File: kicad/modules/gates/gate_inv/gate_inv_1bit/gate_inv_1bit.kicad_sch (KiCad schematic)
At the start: 2 parts, among them Q101 PMOS, Q102 NMOS

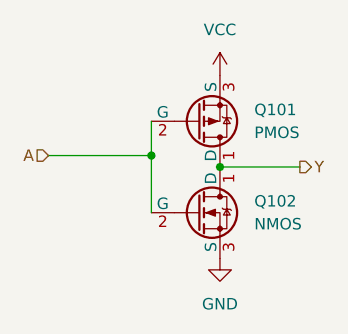
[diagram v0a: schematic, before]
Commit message: feat: complete circuit designs for all ALU components
* Designed all gate modules: AND, OR, NOT, NAND, NOR, XOR (1-bit and 8-bit variants)

* Completed multiplexer hierarchy: 2:1, 4:1, and 8:1 8-bit muxes

* Finalized add_sub board schematic and LED panel designs

* Added new board modules: flags, main_control, main_logic

* Updated Logisim top-level ALU circuit

* Note: KiCad directory path errors to be resolved next (iCloud sync issue), then begin PCB routing
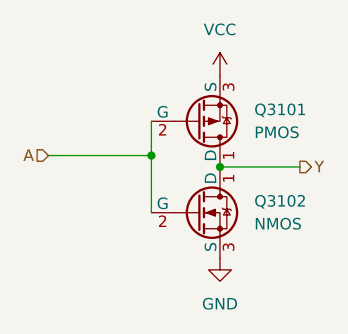
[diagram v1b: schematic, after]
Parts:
- renumbered Q101 to Q3101, Q102 to Q3102
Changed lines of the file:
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@@
 		(dnp no)
 		(fields_autoplaced yes)
-		(property "Reference" "Q102"
+		(property "Reference" "Q3102"
 			(at 102.87 63.4999 0)
 			(effects
@@
 		)
 		(instances
-			(project ""
-				(path "/91c6beb6-7f64-405a-ad9b-2f4d375cbae0"
-					(reference "Q102")
+			(project "main_logic"
+				(path "/9c59990f-2fe5-4da7-bc07-d03b445b1465/99dbd45c-8760-4ff5-9139-add98e67407e"
+					(reference "Q3102")
+					(unit 1)
+				)
+			)
+			(project "main_logic"
+				(path "/e2bb65ff-e340-4712-a878-121a5433abf0/c953f248-6ec6-4063-88a9-6cf78c9a3ffe"
+					(reference "Q3102")
 					(unit 1)
 				)
@@
 		(dnp no)
 		(fields_autoplaced yes)
-		(property "Reference" "#PWR0101"
+		(property "Reference" "#PWR03102"
 			(at 99.06 76.2 0)
 			(effects
@@
 		)
 		(instances
-			(project ""
-				(path "/91c6beb6-7f64-405a-ad9b-2f4d375cbae0"
-					(reference "#PWR0101")
+			(project "main_logic"
+				(path "/9c59990f-2fe5-4da7-bc07-d03b445b1465/99dbd45c-8760-4ff5-9139-add98e67407e"
+					(reference "#PWR03102")
+					(unit 1)
+				)
+			)
+			(project "main_logic"
+				(path "/e2bb65ff-e340-4712-a878-121a5433abf0/c953f248-6ec6-4063-88a9-6cf78c9a3ffe"
+					(reference "#PWR03102")
 					(unit 1)
 				)
@@
 		(dnp no)
 		(fields_autoplaced yes)
-		(property "Reference" "Q101"
+		(property "Reference" "Q3101"
 			(at 102.87 53.3399 0)
 			(effects
@@
 		)
 		(instances
-			(project ""
-				(path "/91c6beb6-7f64-405a-ad9b-2f4d375cbae0"
-					(reference "Q101")
+			(project "main_logic"
+				(path "/9c59990f-2fe5-4da7-bc07-d03b445b1465/99dbd45c-8760-4ff5-9139-add98e67407e"
+					(reference "Q3101")
+					(unit 1)
+				)
+			)
+			(project "main_logic"
+				(path "/e2bb65ff-e340-4712-a878-121a5433abf0/c953f248-6ec6-4063-88a9-6cf78c9a3ffe"
+					(reference "Q3101")
 					(unit 1)
 				)
@@
 		(dnp no)
 		(fields_autoplaced yes)
-		(property "Reference" "#PWR0102"
+		(property "Reference" "#PWR03101"
 			(at 99.06 53.34 0)
 			(effects
@@
 		)
 		(instances
-			(project ""
-				(path "/91c6beb6-7f64-405a-ad9b-2f4d375cbae0"
-					(reference "#PWR0102")
+			(project "main_logic"
+				(path "/9c59990f-2fe5-4da7-bc07-d03b445b1465/99dbd45c-8760-4ff5-9139-add98e67407e"
+					(reference "#PWR03101")
+					(unit 1)
+				)
+			)
+			(project "main_logic"
+				(path "/e2bb65ff-e340-4712-a878-121a5433abf0/c953f248-6ec6-4063-88a9-6cf78c9a3ffe"
+					(reference "#PWR03101")
 					(unit 1)
 				)
@@
 		)
 	)
-	(sheet_instances
-		(path "/"
-			(page "1")
-		)
-	)
-	(embedded_fonts no)
 )

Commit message: Fix KiCad file paths and complete core circuit design
- Fixed file path errors across all KiCad schematics and projects
- Completed core circuit designs:
  * Adder and subtractor modules (adder2, adder8)
  * LED panels (led_panel_1) with display circuits
  * Flag LED circuits for status indicators
  * All dependent logic gate modules (AND, OR, NOT, NAND, NOR, XOR)
  * All multiplexer modules (2:1, 4:1, 8:1, 8-bit)
  * Main control board schematics
  * Flags board schematics
- Updated .gitignore to exclude KiCad backups, cache files, and lock files
- Ready for pin placement and routing of control buses, power rails, and inter-board signals
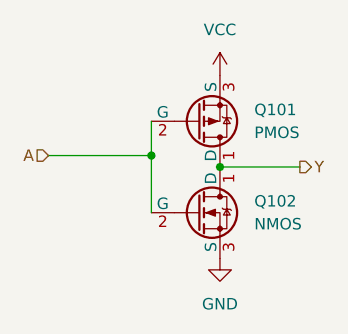
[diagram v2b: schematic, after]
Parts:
- renumbered Q3101 to Q101, Q3102 to Q102
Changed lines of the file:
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@@
 		(dnp no)
 		(fields_autoplaced yes)
-		(property "Reference" "Q3102"
+		(property "Reference" "Q102"
 			(at 102.87 63.4999 0)
 			(effects
@@
 		)
 		(instances
-			(project "main_logic"
-				(path "/9c59990f-2fe5-4da7-bc07-d03b445b1465/99dbd45c-8760-4ff5-9139-add98e67407e"
-					(reference "Q3102")
-					(unit 1)
-				)
-			)
-			(project "main_logic"
-				(path "/e2bb65ff-e340-4712-a878-121a5433abf0/c953f248-6ec6-4063-88a9-6cf78c9a3ffe"
-					(reference "Q3102")
+			(project "gate_inv_8bit"
+				(path "/d141fce1-7092-474f-ac13-21228438d92c/12baccda-de61-4ff2-89c1-cc980ff8bc59"
+					(reference "Q402")
+					(unit 1)
+				)
+				(path "/d141fce1-7092-474f-ac13-21228438d92c/3a2fa2a6-4027-46c4-90cc-58cbe339a8cc"
+					(reference "Q302")
+					(unit 1)
+				)
+				(path "/d141fce1-7092-474f-ac13-21228438d92c/60421d18-f918-422e-9acf-6291f4552ab2"
+					(reference "Q102")
+					(unit 1)
+				)
+				(path "/d141fce1-7092-474f-ac13-21228438d92c/7ca7b9d9-dd96-40f5-80e5-151f81d53068"
+					(reference "Q502")
+					(unit 1)
+				)
+				(path "/d141fce1-7092-474f-ac13-21228438d92c/cbe845e2-fbfa-4e99-b5aa-42ea773ed407"
+					(reference "Q802")
+					(unit 1)
+				)
+				(path "/d141fce1-7092-474f-ac13-21228438d92c/cfb92fbf-905c-43ce-8707-6acd4a04428b"
+					(reference "Q602")
+					(unit 1)
+				)
+				(path "/d141fce1-7092-474f-ac13-21228438d92c/e8076ae0-d234-4675-a580-3fff14bf2f4c"
+					(reference "Q702")
 					(unit 1)
 				)
@@
 		(dnp no)
 		(fields_autoplaced yes)
-		(property "Reference" "#PWR03102"
+		(property "Reference" "#PWR0102"
 			(at 99.06 76.2 0)
 			(effects
@@
 		)
 		(instances
-			(project "main_logic"
-				(path "/9c59990f-2fe5-4da7-bc07-d03b445b1465/99dbd45c-8760-4ff5-9139-add98e67407e"
-					(reference "#PWR03102")
-					(unit 1)
-				)
-			)
-			(project "main_logic"
-				(path "/e2bb65ff-e340-4712-a878-121a5433abf0/c953f248-6ec6-4063-88a9-6cf78c9a3ffe"
-					(reference "#PWR03102")
+			(project "gate_inv_8bit"
+				(path "/d141fce1-7092-474f-ac13-21228438d92c/12baccda-de61-4ff2-89c1-cc980ff8bc59"
+					(reference "#PWR0402")
+					(unit 1)
+				)
+				(path "/d141fce1-7092-474f-ac13-21228438d92c/3a2fa2a6-4027-46c4-90cc-58cbe339a8cc"
+					(reference "#PWR0302")
+					(unit 1)
+				)
+				(path "/d141fce1-7092-474f-ac13-21228438d92c/60421d18-f918-422e-9acf-6291f4552ab2"
+					(reference "#PWR0102")
+					(unit 1)
+				)
+				(path "/d141fce1-7092-474f-ac13-21228438d92c/7ca7b9d9-dd96-40f5-80e5-151f81d53068"
+					(reference "#PWR0502")
+					(unit 1)
+				)
+				(path "/d141fce1-7092-474f-ac13-21228438d92c/cbe845e2-fbfa-4e99-b5aa-42ea773ed407"
+					(reference "#PWR0802")
+					(unit 1)
+				)
+				(path "/d141fce1-7092-474f-ac13-21228438d92c/cfb92fbf-905c-43ce-8707-6acd4a04428b"
+					(reference "#PWR0602")
+					(unit 1)
+				)
+				(path "/d141fce1-7092-474f-ac13-21228438d92c/e8076ae0-d234-4675-a580-3fff14bf2f4c"
+					(reference "#PWR0702")
 					(unit 1)
 				)
@@
 		(dnp no)
 		(fields_autoplaced yes)
-		(property "Reference" "Q3101"
+		(property "Reference" "Q101"
 			(at 102.87 53.3399 0)
 			(effects
@@
 		)
 		(instances
-			(project "main_logic"
-				(path "/9c59990f-2fe5-4da7-bc07-d03b445b1465/99dbd45c-8760-4ff5-9139-add98e67407e"
-					(reference "Q3101")
-					(unit 1)
-				)
-			)
-			(project "main_logic"
-				(path "/e2bb65ff-e340-4712-a878-121a5433abf0/c953f248-6ec6-4063-88a9-6cf78c9a3ffe"
-					(reference "Q3101")
+			(project "gate_inv_8bit"
+				(path "/d141fce1-7092-474f-ac13-21228438d92c/12baccda-de61-4ff2-89c1-cc980ff8bc59"
+					(reference "Q401")
+					(unit 1)
+				)
+				(path "/d141fce1-7092-474f-ac13-21228438d92c/3a2fa2a6-4027-46c4-90cc-58cbe339a8cc"
+					(reference "Q301")
+					(unit 1)
+				)
+				(path "/d141fce1-7092-474f-ac13-21228438d92c/60421d18-f918-422e-9acf-6291f4552ab2"
+					(reference "Q101")
+					(unit 1)
+				)
+				(path "/d141fce1-7092-474f-ac13-21228438d92c/7ca7b9d9-dd96-40f5-80e5-151f81d53068"
+					(reference "Q501")
+					(unit 1)
+				)
+				(path "/d141fce1-7092-474f-ac13-21228438d92c/cbe845e2-fbfa-4e99-b5aa-42ea773ed407"
+					(reference "Q801")
+					(unit 1)
+				)
+				(path "/d141fce1-7092-474f-ac13-21228438d92c/cfb92fbf-905c-43ce-8707-6acd4a04428b"
+					(reference "Q601")
+					(unit 1)
+				)
+				(path "/d141fce1-7092-474f-ac13-21228438d92c/e8076ae0-d234-4675-a580-3fff14bf2f4c"
+					(reference "Q701")
 					(unit 1)
 				)
@@
 		(dnp no)
 		(fields_autoplaced yes)
-		(property "Reference" "#PWR03101"
+		(property "Reference" "#PWR0101"
 			(at 99.06 53.34 0)
 			(effects
@@
 		)
 		(instances
-			(project "main_logic"
-				(path "/9c59990f-2fe5-4da7-bc07-d03b445b1465/99dbd45c-8760-4ff5-9139-add98e67407e"
-					(reference "#PWR03101")
-					(unit 1)
-				)
-			)
-			(project "main_logic"
-				(path "/e2bb65ff-e340-4712-a878-121a5433abf0/c953f248-6ec6-4063-88a9-6cf78c9a3ffe"
-					(reference "#PWR03101")
-					(unit 1)
-				)
+			(project "gate_inv_8bit"
+				(path "/d141fce1-7092-474f-ac13-21228438d92c/12baccda-de61-4ff2-89c1-cc980ff8bc59"
+					(reference "#PWR0401")
+					(unit 1)
+				)
+				(path "/d141fce1-7092-474f-ac13-21228438d92c/3a2fa2a6-4027-46c4-90cc-58cbe339a8cc"
+					(reference "#PWR0301")
+					(unit 1)
+				)
+				(path "/d141fce1-7092-474f-ac13-21228438d92c/60421d18-f918-422e-9acf-6291f4552ab2"
+					(reference "#PWR0101")
+					(unit 1)
+				)
+				(path "/d141fce1-7092-474f-ac13-21228438d92c/7ca7b9d9-dd96-40f5-80e5-151f81d53068"
+					(reference "#PWR0501")
+					(unit 1)
+				)
+				(path "/d141fce1-7092-474f-ac13-21228438d92c/cbe845e2-fbfa-4e99-b5aa-42ea773ed407"
+					(reference "#PWR0801")
+					(unit 1)
+				)
+				(path "/d141fce1-7092-474f-ac13-21228438d92c/cfb92fbf-905c-43ce-8707-6acd4a04428b"
+					(reference "#PWR0601")
+					(unit 1)
+				)
+				(path "/d141fce1-7092-474f-ac13-21228438d92c/e8076ae0-d234-4675-a580-3fff14bf2f4c"
+					(reference "#PWR0701")
+					(unit 1)
+				)
